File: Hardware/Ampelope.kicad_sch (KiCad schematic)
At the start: 14 parts, among them J1 B_In, J3 Eurorack_10_pin_power, J4 RM_OUT, U1 TL074

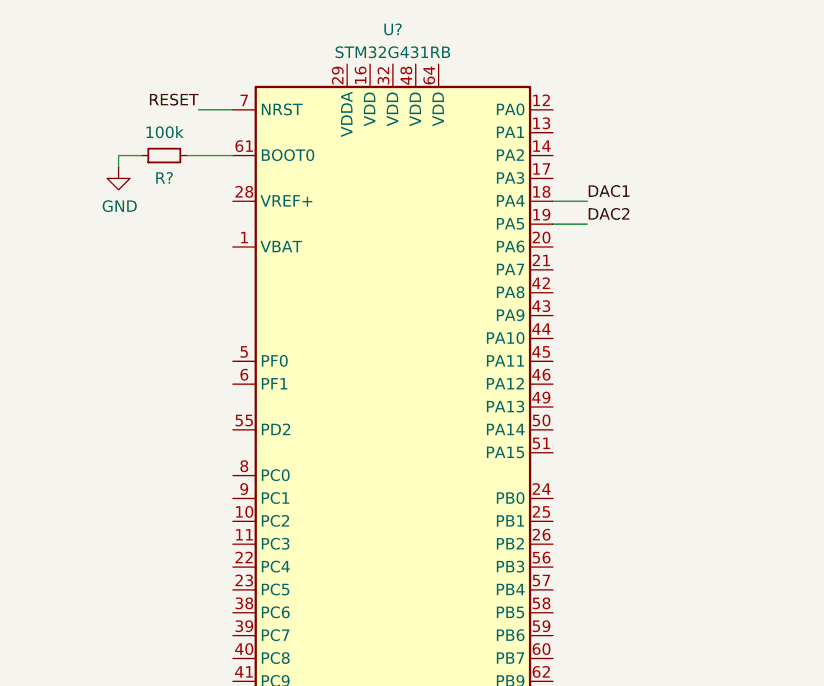
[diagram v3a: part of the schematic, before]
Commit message: Added additional DAC/Opamp channel
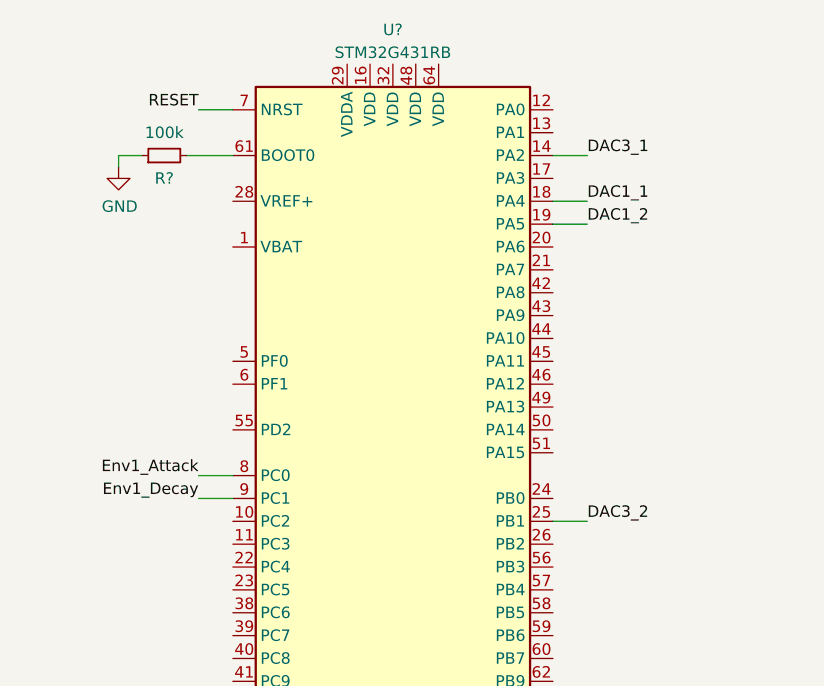
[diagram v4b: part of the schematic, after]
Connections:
- net DAC3_1: now reaches U?.14 (PA2)
- net DAC3_2: now reaches U?.25 (PB1)
- net Env1_Attack: now reaches U?.8 (PC0)
- net Env1_Decay: now reaches U?.9 (PC1)
- net DAC1 renamed DAC1_1
- net DAC2 renamed DAC1_2
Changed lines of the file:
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@@
+    (stroke (width 0) (type solid) (color 0 0 0 0))
+  )
+  (wire (pts (xy 45.72 81.28) (xy 41.91 81.28))
+    (stroke (width 0) (type solid) (color 0 0 0 0))
+  )
+  (wire (pts (xy 45.72 83.82) (xy 41.91 83.82))
     (stroke (width 0) (type solid) (color 0 0 0 0))
   )
@@
     (stroke (width 0) (type solid) (color 0 0 0 0))
   )
+  (wire (pts (xy 81.28 45.72) (xy 85.09 45.72))
+    (stroke (width 0) (type solid) (color 0 0 0 0))
+  )
   (wire (pts (xy 81.28 50.8) (xy 85.09 50.8))
     (stroke (width 0) (type solid) (color 0 0 0 0))
   )
   (wire (pts (xy 81.28 53.34) (xy 85.09 53.34))
+    (stroke (width 0) (type solid) (color 0 0 0 0))
+  )
+  (wire (pts (xy 81.28 86.36) (xy 85.09 86.36))
     (stroke (width 0) (type solid) (color 0 0 0 0))
   )
@@
     (effects (font (size 1.27 1.27)) (justify right bottom))
   )
-  (label "DAC1" (at 85.09 50.8 0)
+  (label "Env1_Attack" (at 41.91 81.28 180)
+    (effects (font (size 1.27 1.27)) (justify right bottom))
+  )
+  (label "Env1_Decay" (at 41.91 83.82 180)
+    (effects (font (size 1.27 1.27)) (justify right bottom))
+  )
+  (label "DAC3_1" (at 85.09 45.72 0)
     (effects (font (size 1.27 1.27)) (justify left bottom))
   )
-  (label "DAC2" (at 85.09 53.34 0)
+  (label "DAC1_1" (at 85.09 50.8 0)
     (effects (font (size 1.27 1.27)) (justify left bottom))
   )
+  (label "DAC1_2" (at 85.09 53.34 0)
+    (effects (font (size 1.27 1.27)) (justify left bottom))
+  )
+  (label "DAC3_2" (at 85.09 86.36 0)
+    (effects (font (size 1.27 1.27)) (justify left bottom))
+  )
